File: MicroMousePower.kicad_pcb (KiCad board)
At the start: 2 copper layers, 58.4 x 53.8 mm, 103 parts, among them J1 USB_C_Receptacle_PowerOnly_6P, J2 Conn_02x16_Odd_Even, J3 Conn_01x02_Pin, Q1 TIP41C, Q2 TIP41C, Q3 TIP41C, U1 INA219AxDCN, U2 MCP73831-3-MC, U3 CH224K, U4 DRV8833PWPR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

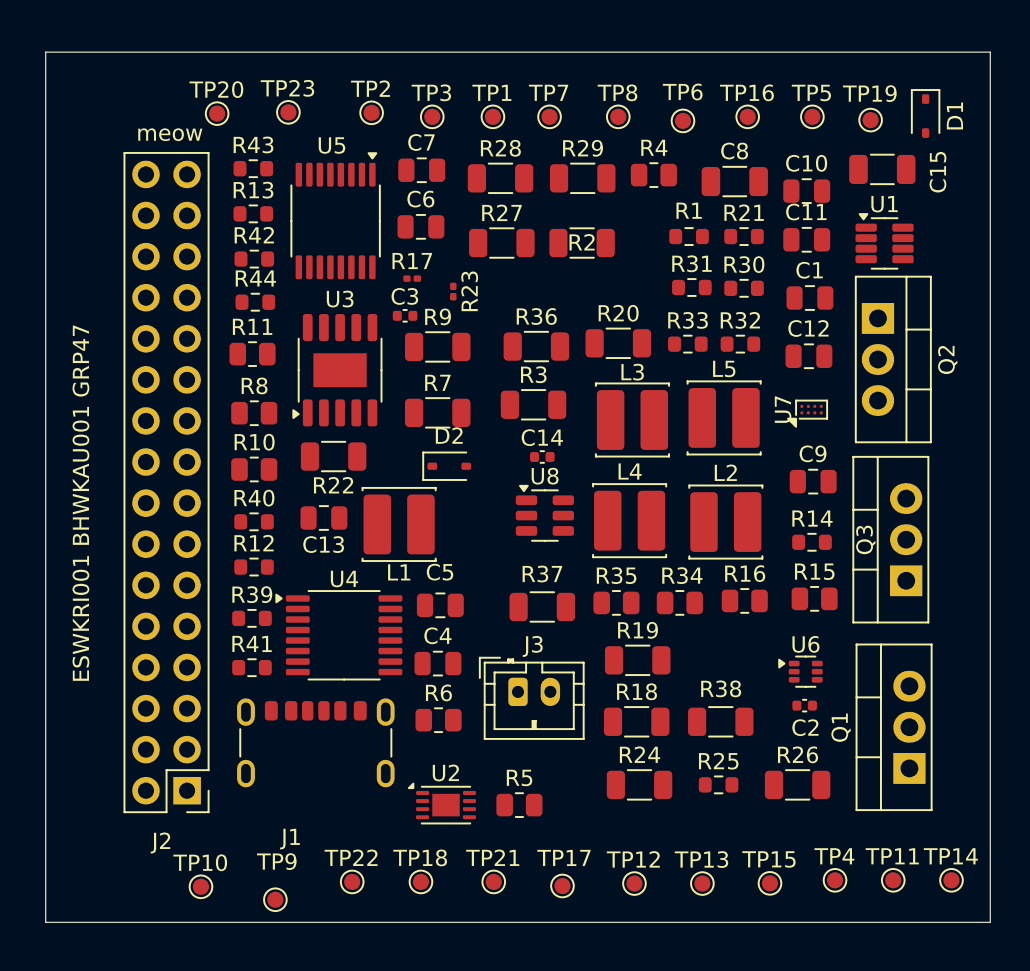
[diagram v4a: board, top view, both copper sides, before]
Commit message: rotated for bending
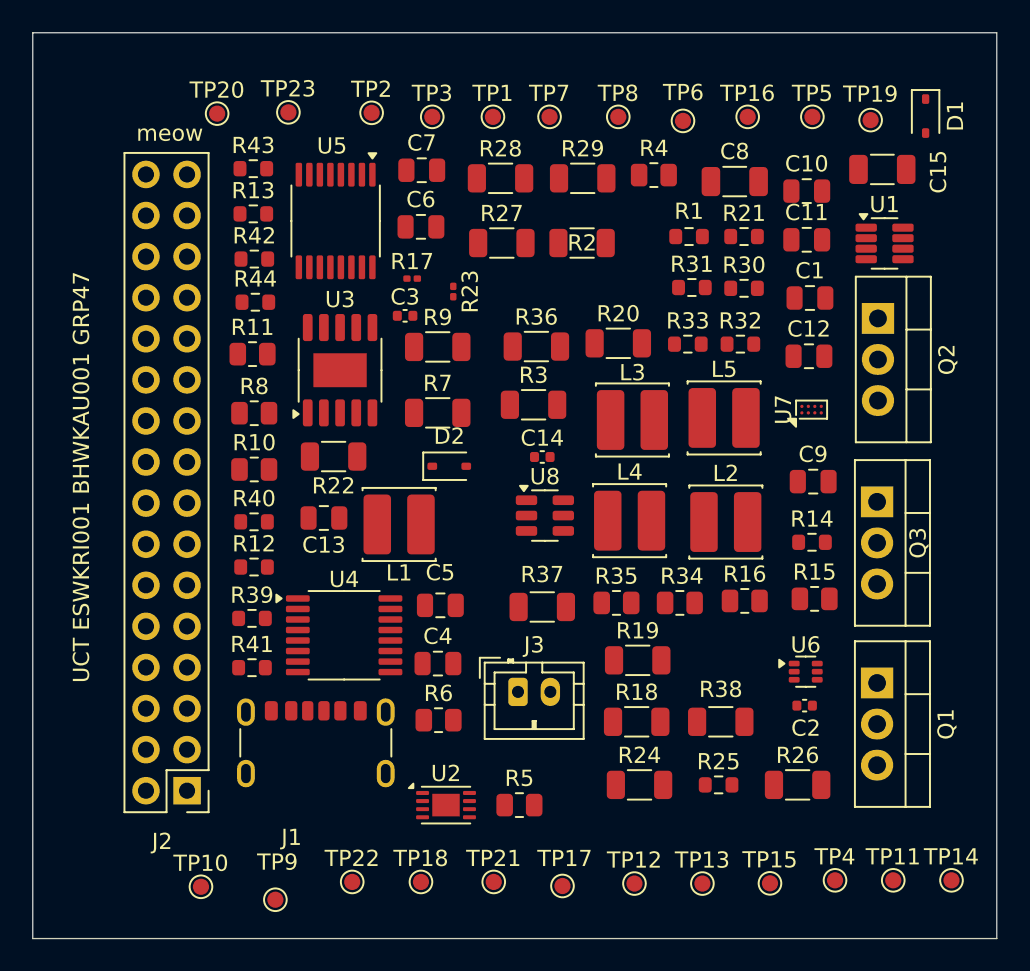
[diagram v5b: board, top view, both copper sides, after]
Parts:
- moved Q1 5.65 mm to (195.2, 102.2), turned to -90 degrees
- moved Q3 5.20 mm to (195.2, 91.0), turned to -90 degrees
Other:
- board size 58.4 x 53.8 mm -> 59.6 x 56 mm
- board text added: "UCT ESWKRI001 BHWKAU001 GRP47"
- board text removed: "ESWKRI001 BHWKAU001 GRP47"
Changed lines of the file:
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@@
 	(footprint "Package_TO_SOT_THT:TO-220-3_Vertical"
 		(layer "F.Cu")
-		(at 197 95.88 90)
+		(at 195.2 91 -90)
 		(descr "TO-220-3, Vertical, RM 2.54mm, see https://www.vishay.com/docs/66542/to-220-1.pdf")
 		(tags "TO-220-3 Vertical RM 2.54mm")
@@
 		)
 		(property "LCSC" "C92603"
-			(at 0 0 90)
+			(at 0 0 270)
 			(unlocked yes)
 			(layer "F.Fab")
@@
 		(attr through_hole)
 		(fp_line
-			(start 7.66 -3.27)
+			(start -2.58 1.371)
 			(end 7.66 1.371)
 			(stroke
@@
 		)
 		(fp_line
-			(start 4.391 -3.27)
-			(end 4.391 -1.76)
+			(start -2.58 -1.76)
+			(end 7.66 -1.76)
 			(stroke
 				(width 0.12)
@@
 		)
 		(fp_line
-			(start 0.69 -3.27)
-			(end 0.69 -1.76)
+			(start -2.58 -3.27)
+			(end -2.58 1.371)
 			(stroke
 				(width 0.12)
@@
 		)
 		(fp_line
-			(start -2.58 -3.27)
-			(end -2.58 1.371)
+			(start 0.69 -3.27)
+			(end 0.69 -1.76)
 			(stroke
 				(width 0.12)
@@
 		)
 		(fp_line
-			(start -2.58 -1.76)
-			(end 7.66 -1.76)
+			(start 4.391 -3.27)
+			(end 4.391 -1.76)
 			(stroke
 				(width 0.12)
@@
 		)
 		(fp_line
-			(start -2.58 1.371)
+			(start 7.66 -3.27)
 			(end 7.66 1.371)
 			(stroke
@@
 		)
 		(fp_line
-			(start 7.79 -3.4)
-			(end -2.71 -3.4)
+			(start -2.71 1.51)
+			(end 7.79 1.51)
 			(stroke
 				(width 0.05)
@@
 		)
 		(fp_line
-			(start -2.71 -3.4)
-			(end -2.71 1.51)
+			(start 7.79 1.51)
+			(end 7.79 -3.4)
 			(stroke
 				(width 0.05)
@@
 		)
 		(fp_line
-			(start 7.79 1.51)
-			(end 7.79 -3.4)
+			(start -2.71 -3.4)
+			(end -2.71 1.51)
 			(stroke
 				(width 0.05)
@@
 		)
 		(fp_line
-			(start -2.71 1.51)
-			(end 7.79 1.51)
+			(start 7.79 -3.4)
+			(end -2.71 -3.4)
 			(stroke
 				(width 0.05)
@@
 		)
 		(fp_line
-			(start 7.54 -3.15)
-			(end -2.46 -3.15)
+			(start -2.46 1.25)
+			(end 7.54 1.25)
 			(stroke
 				(width 0.1)
@@
 		)
 		(fp_line
-			(start 4.39 -3.15)
-			(end 4.39 -1.88)
+			(start 7.54 1.25)
+			(end 7.54 -3.15)
 			(stroke
 				(width 0.1)
@@
 		)
 		(fp_line
-			(start 0.69 -3.15)
-			(end 0.69 -1.88)
+			(start -2.46 -1.88)
+			(end 7.54 -1.88)
 			(stroke
 				(width 0.1)
@@
 		)
 		(fp_line
-			(start -2.46 -1.88)
-			(end 7.54 -1.88)
+			(start 0.69 -3.15)
+			(end 0.69 -1.88)
 			(stroke
 				(width 0.1)
@@
 		)
 		(fp_line
-			(start 7.54 1.25)
-			(end 7.54 -3.15)
+			(start 4.39 -3.15)
+			(end 4.39 -1.88)
 			(stroke
 				(width 0.1)
@@
 		)
 		(fp_line
-			(start -2.46 1.25)
-			(end 7.54 1.25)
+			(start 7.54 -3.15)
+			(end -2.46 -3.15)
 			(stroke
 				(width 0.1)
@@
 		)
 		(pad "1" thru_hole rect
-			(at 0 0 90)
+			(at 0 0 270)
 			(size 1.905 2)
 			(drill 1.1)
@@
 		)
 		(pad "2" thru_hole oval
-			(at 2.54 0 90)
+			(at 2.54 0 270)
 			(size 1.905 2)
 			(drill 1.1)
@@
 		)
 		(pad "3" thru_hole oval
-			(at 5.08 0 90)
+			(at 5.08 0 270)
 			(size 1.905 2)
 			(drill 1.1)
@@
 	(footprint "Package_TO_SOT_THT:TO-220-3_Vertical"
 		(layer "F.Cu")
-		(at 197.2 107.48 90)
+		(at 195.2 102.2 -90)
 		(descr "TO-220-3, Vertical, RM 2.54mm, see https://www.vishay.com/docs/66542/to-220-1.pdf")
 		(tags "TO-220-3 Vertical RM 2.54mm")
@@
 		)
 		(property "LCSC" "C92603"
-			(at 0 0 90)
+			(at 0 0 270)
 			(unlocked yes)
 			(layer "F.Fab")
@@
 		(attr through_hole)
 		(fp_line
-			(start 7.66 -3.27)
+			(start -2.58 1.371)
 			(end 7.66 1.371)
 			(stroke
@@
 		)
 		(fp_line
-			(start 4.391 -3.27)
-			(end 4.391 -1.76)
+			(start -2.58 -1.76)
+			(end 7.66 -1.76)
 			(stroke
 				(width 0.12)
@@
 		)
 		(fp_line
-			(start 0.69 -3.27)
-			(end 0.69 -1.76)
+			(start -2.58 -3.27)
+			(end -2.58 1.371)
 			(stroke
 				(width 0.12)
@@
 		)
 		(fp_line
-			(start -2.58 -3.27)
-			(end -2.58 1.371)
+			(start 0.69 -3.27)
+			(end 0.69 -1.76)
 			(stroke
 				(width 0.12)
@@
 		)
 		(fp_line
-			(start -2.58 -1.76)
-			(end 7.66 -1.76)
+			(start 4.391 -3.27)
+			(end 4.391 -1.76)
 			(stroke
 				(width 0.12)
@@
 		)
 		(fp_line
-			(start -2.58 1.371)
+			(start 7.66 -3.27)
 			(end 7.66 1.371)
 			(stroke
@@
 		)
 		(fp_line
-			(start 7.79 -3.4)
-			(end -2.71 -3.4)
+			(start -2.71 1.51)
+			(end 7.79 1.51)
 			(stroke
 				(width 0.05)
@@
 		)
 		(fp_line
-			(start -2.71 -3.4)
-			(end -2.71 1.51)
+			(start 7.79 1.51)
+			(end 7.79 -3.4)
 			(stroke
 				(width 0.05)
@@
 		)
 		(fp_line
-			(start 7.79 1.51)
-			(end 7.79 -3.4)
+			(start -2.71 -3.4)
+			(end -2.71 1.51)
 			(stroke
 				(width 0.05)
@@
 		)
 		(fp_line
-			(start -2.71 1.51)
-			(end 7.79 1.51)
+			(start 7.79 -3.4)
+			(end -2.71 -3.4)
 			(stroke
 				(width 0.05)
@@
 		)
 		(fp_line
-			(start 7.54 -3.15)
-			(end -2.46 -3.15)
+			(start -2.46 1.25)
+			(end 7.54 1.25)
 			(stroke
 				(width 0.1)
@@
 		)
 		(fp_line
-			(start 4.39 -3.15)
-			(end 4.39 -1.88)
+			(start 7.54 1.25)
+			(end 7.54 -3.15)
 			(stroke
 				(width 0.1)
@@
 		)
 		(fp_line
-			(start 0.69 -3.15)
-			(end 0.69 -1.88)
+			(start -2.46 -1.88)
+			(end 7.54 -1.88)
 			(stroke
 				(width 0.1)
@@
 		)
 		(fp_line
-			(start -2.46 -1.88)
-			(end 7.54 -1.88)
+			(start 0.69 -3.15)
+			(end 0.69 -1.88)
 			(stroke
 				(width 0.1)
@@
 		)
 		(fp_line
-			(start 7.54 1.25)
-			(end 7.54 -3.15)
+			(start 4.39 -3.15)
+			(end 4.39 -1.88)
 			(stroke
 				(width 0.1)
@@
 		)
 		(fp_line
-			(start -2.46 1.25)
-			(end 7.54 1.25)
+			(start 7.54 -3.15)
+			(end -2.46 -3.15)
 			(stroke
 				(width 0.1)
@@
 		)
 		(pad "1" thru_hole rect
-			(at 0 0 90)
+			(at 0 0 270)
 			(size 1.905 2)
 			(drill 1.1)
@@
 		)
 		(pad "2" thru_hole oval
-			(at 2.54 0 90)
+			(at 2.54 0 270)
 			(size 1.905 2)
 			(drill 1.1)
@@
 		)
 		(pad "3" thru_hole oval
-			(at 5.08 0 90)
+			(at 5.08 0 270)
 			(size 1.905 2)
 			(drill 1.1)
@@
 	)
 	(gr_rect
-		(start 143.8 63.2)
-		(end 202.2 117)
+		(start 143 62)
+		(end 202.6 118)
 		(stroke
 			(width 0.05)
@@
 		(layer "Edge.Cuts")
 	)
-	(gr_text "ESWKRI001 BHWKAU001 GRP47"
+	(gr_text "UCT ESWKRI001 BHWKAU001 GRP47"
 		(at 146.6 102.2 90)
 		(layer "F.SilkS")

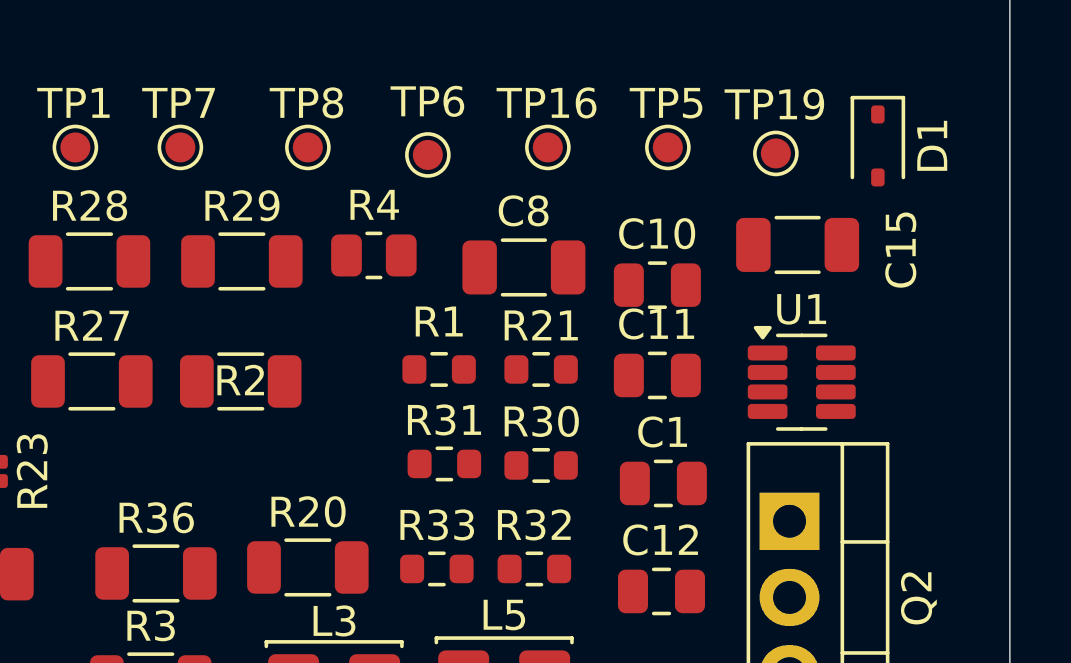
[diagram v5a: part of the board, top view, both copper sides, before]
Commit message: moved resistors to overcome disconnect
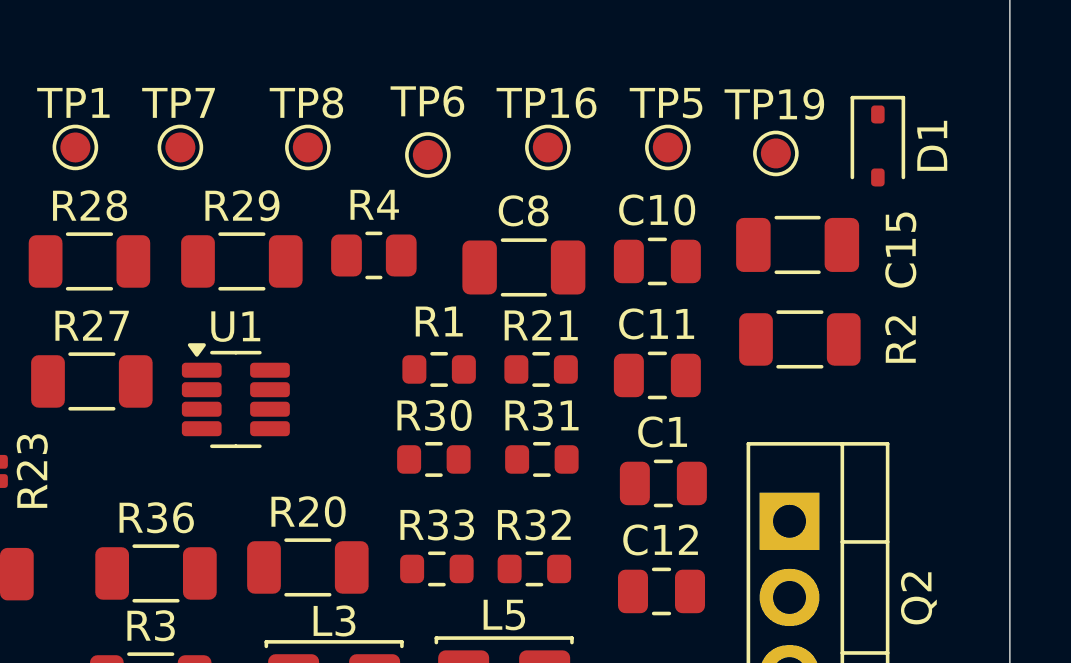
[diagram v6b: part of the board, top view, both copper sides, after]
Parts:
- moved U1 18.9 mm to (176.8, 75.6)
- moved R2 18.7 mm to (195.6, 73.6)
- moved R30 3.58 mm to (183.4, 77.6)
- moved R31 3.25 mm to (187.0, 77.6)
- moved C10 0.79 mm to (190.8, 71.0)
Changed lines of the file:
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@@
 	(footprint "Capacitor_SMD:C_0805_2012Metric"
 		(layer "F.Cu")
-		(at 190.85 71.79)
+		(at 190.85 71)
 		(descr "Capacitor SMD 0805 (2012 Metric), square (rectangular) end terminal, IPC_7351 nominal, (Body size source: IPC-SM-782 page 76, https://www.pcb-3d.com/wordpress/wp-content/uploads/ipc-sm-782a_amendment_1_and_2.pdf, https://docs.google.com/spreadsheets/d/1BsfQQcO9C6DZCsRaXUlFlo91Tg2WpOkGARC1WS5S8t0/edit?usp=sharing), generated with kicad-footprint-generator")
 		(tags "capacitor")
@@
 	(footprint "Resistor_SMD:R_1206_3216Metric"
 		(layer "F.Cu")
-		(at 176.9625 75 180)
+		(at 195.6 73.6 180)
 		(descr "Resistor SMD 1206 (3216 Metric), square (rectangular) end terminal, IPC_7351 nominal, (Body size source: IPC-SM-782 page 72, https://www.pcb-3d.com/wordpress/wp-content/uploads/ipc-sm-782a_amendment_1_and_2.pdf), generated with kicad-footprint-generator")
 		(tags "resistor")
 		(property "Reference" "R2"
-			(at 0 0 0)
+			(at -3.4 0 90)
 			(layer "F.SilkS")
 			(effects
@@
 	(footprint "Package_TO_SOT_SMD:SOT-23-8"
 		(layer "F.Cu")
-		(at 195.6625 75.025)
+		(at 176.8 75.6)
 		(descr "SOT, 8 Pin (JEDEC MO-178 Var BA https://www.jedec.org/document_search?search_api_views_fulltext=MO-178), generated with kicad-footprint-generator ipc_gullwing_generator.py")
 		(tags "SOT TO_SOT_SMD")
@@
 	(footprint "Resistor_SMD:R_0603_1608Metric"
 		(layer "F.Cu")
-		(at 186.975 77.8)
+		(at 183.4 77.6)
 		(descr "Resistor SMD 0603 (1608 Metric), square (rectangular) end terminal, IPC_7351 nominal, (Body size source: IPC-SM-782 page 72, https://www.pcb-3d.com/wordpress/wp-content/uploads/ipc-sm-782a_amendment_1_and_2.pdf), generated with kicad-footprint-generator")
 		(tags "resistor")
@@
 	(footprint "Resistor_SMD:R_0603_1608Metric"
 		(layer "F.Cu")
-		(at 183.75 77.75)
+		(at 187 77.6)
 		(descr "Resistor SMD 0603 (1608 Metric), square (rectangular) end terminal, IPC_7351 nominal, (Body size source: IPC-SM-782 page 72, https://www.pcb-3d.com/wordpress/wp-content/uploads/ipc-sm-782a_amendment_1_and_2.pdf), generated with kicad-footprint-generator")
 		(tags "resistor")
